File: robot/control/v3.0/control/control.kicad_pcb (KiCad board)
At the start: 2 copper layers, 0 parts

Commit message: footprint selection done, placement work
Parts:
- added BZ1: MLT-5020, AT-Buzzer:MLT-5020, F.Cu at (157.6, 175.0)
- added C1: 100n 50V, Capacitor_SMD:C_0402_1005Metric, F.Cu at (-61.0, 71.5)
- added C10: 100n 50V, Capacitor_SMD:C_0402_1005Metric, F.Cu at (-58.1, 75.5)
- added C11: 11pF, Capacitor_SMD:C_0402_1005Metric, B.Cu at (174.6, 108.3)
- added C12: 11pF, Capacitor_SMD:C_0402_1005Metric, B.Cu at (172.6, 108.3)
- added C13: 100n 50V, Capacitor_SMD:C_0402_1005Metric, F.Cu at (-58.1, 81.4)
- added C14: 2.2uF 10V, Capacitor_SMD:C_0603_1608Metric, F.Cu at (-30.6, 56.7)
- added C15: 2.2uF 10V, Capacitor_SMD:C_0603_1608Metric, F.Cu at (-30.6, 59.2)
- added C16: 100n 50V, Capacitor_SMD:C_0402_1005Metric, F.Cu at (-58.1, 83.3)
- added C17: 100n 50V, Capacitor_SMD:C_0402_1005Metric, F.Cu at (-55.2, 71.5)
- added C18: 100n 50V, Capacitor_SMD:C_0402_1005Metric, F.Cu at (-55.2, 73.5)
- added C19: 100n 50V, Capacitor_SMD:C_0402_1005Metric, F.Cu at (-55.2, 75.5)
- added C2: 1u 50V, Capacitor_SMD:C_0402_1005Metric, F.Cu at (-61.0, 73.5)
- added C20: 100n 50V, Capacitor_SMD:C_0402_1005Metric, F.Cu at (-55.2, 77.4)
- added C21: 100n 50V, Capacitor_SMD:C_0402_1005Metric, F.Cu at (-55.2, 79.4)
- added C22: 100n 50V, Capacitor_SMD:C_0402_1005Metric, F.Cu at (-55.2, 81.4)
- added C23: 100n 50V, Capacitor_SMD:C_0402_1005Metric, F.Cu at (-55.2, 83.3)
- added C24: 100n 50V, Capacitor_SMD:C_0402_1005Metric, F.Cu at (-52.3, 71.5)
- added C25: 100n 50V, Capacitor_SMD:C_0402_1005Metric, F.Cu at (-52.3, 73.5)
- added C26: 100n 50V, Capacitor_SMD:C_0402_1005Metric, F.Cu at (-52.3, 75.5)
- added C27: 100n 50V, Capacitor_SMD:C_0402_1005Metric, F.Cu at (-52.3, 77.4)
- added C28: 0.1uF 63V, Capacitor_SMD:C_0402_1005Metric, F.Cu at (154.0, 119.0)
- added C29: 0.1uF 63V, Capacitor_SMD:C_0402_1005Metric, F.Cu at (154.0, 117.0)
- added C3: 15pF, Capacitor_SMD:C_0402_1005Metric, B.Cu at (174.4, 102.6)
- added C30: 0.1u, Capacitor_SMD:C_0402_1005Metric, F.Cu at (-146.9, 131.1)
- added C31: 1u, Capacitor_SMD:C_1206_3216Metric, F.Cu at (-151.2, 127.9)
- added C32: 0.1uF 63V, Capacitor_SMD:C_0402_1005Metric, F.Cu at (-98.8, 77.4)
- added C33: 0.1uF 63V, Capacitor_SMD:C_0402_1005Metric, F.Cu at (-98.8, 79.3)
- added C34: 0.1uF 63V, Capacitor_SMD:C_0402_1005Metric, F.Cu at (-98.8, 81.3)
- added C35: 0.1uF 63V, Capacitor_SMD:C_0402_1005Metric, F.Cu at (-98.8, 83.3)
- added C36: 0.1uF 63V, Capacitor_SMD:C_0402_1005Metric, F.Cu at (-98.8, 85.2)
- added C37: 0.1uF 63V, Capacitor_SMD:C_0402_1005Metric, F.Cu at (-98.8, 87.2)
- added C38: 4.7uF 25V, Capacitor_SMD:C_0805_2012Metric, F.Cu at (163.3, 173.0)
- added C4: 15pF, Capacitor_SMD:C_0402_1005Metric, B.Cu at (172.1, 102.0)
- added C5: 100n 50V, Capacitor_SMD:C_0402_1005Metric, F.Cu at (-61.0, 79.4)
- added C6: 1u 50V, Capacitor_SMD:C_0402_1005Metric, F.Cu at (-61.0, 81.4)
- added C7: 100n 50V, Capacitor_SMD:C_0402_1005Metric, F.Cu at (-61.0, 83.3)
- added C8: 1u 50V, Capacitor_SMD:C_0402_1005Metric, F.Cu at (-58.1, 71.5)
- added C9: 1u 50V, Capacitor_SMD:C_0402_1005Metric, F.Cu at (-58.1, 73.5)
- added D1: SMBJ26CA, AT-Discrete:D_SMB_Non-Polar, F.Cu at (-152.8, 123.5)
- added D10: XL-1608UGC-04, AT-LED:LED0603, F.Cu at (-95.3, 77.7)
- added D11: XL-1608UGC-04, AT-LED:LED0603, F.Cu at (-95.3, 80.2)
- added D12: XL-1608UGC-04, AT-LED:LED0603, F.Cu at (-95.3, 82.8)
- added D13: XL-1608UGC-04, AT-LED:LED0603, F.Cu at (-95.3, 85.3)
- added D2: XL-1608UWC-04, AT-LED:LED0603, F.Cu at (-152.0, 130.8)
- added D3: LTST-C195KGJRKT, AT-LED:LED0606_S_1324, F.Cu at (95.2, 178.5)
- added D4: LTST-C195KGJRKT, AT-LED:LED0606_S_1324, F.Cu at (98.1, 178.5)
- added D5: MHT194YBCT, AT-LED:LED0606_Z_1324, F.Cu at (96.5, 182.9)
- added D6: LTST-C195KGJRKT, AT-LED:LED0606_S_1324, F.Cu at (95.2, 187.0)
- added D7: LTST-C195KGJRKT, AT-LED:LED0606_S_1324, F.Cu at (98.0, 187.0)
- added D8: XL-1608UOC-06, AT-LED:LED0603, F.Cu at (105.0, 134.4)
- added D9: RBR5LAM60ATR, Diode_SMD:D_SOD-128, F.Cu at (157.8, 169.4)
- added F1: 4A, Fuse:Fuse_1206_3216Metric_Pad1.42x1.75mm_HandSolder, F.Cu at (74.1, 128.6)
- added F2: 4A, Fuse:Fuse_1206_3216Metric_Pad1.42x1.75mm_HandSolder, F.Cu at (100.6, 64.9)
- added F3: 4A, Fuse:Fuse_1206_3216Metric_Pad1.42x1.75mm_HandSolder, F.Cu at (209.1, 74.6)
- added F4: 4A, Fuse:Fuse_1206_3216Metric_Pad1.42x1.75mm_HandSolder, F.Cu at (226.2, 142.4)
- added F5: 15A, AT-Fuses:3557-2, F.Cu at (198.5, 131.5)
- added F6: ~, Fuse:Fuse_0603_1608Metric_Pad1.05x0.95mm_HandSolder, F.Cu at (-146.8, 105.4)
- added F7: ~, Fuse:Fuse_0603_1608Metric_Pad1.05x0.95mm_HandSolder, F.Cu at (-146.8, 107.9)
- added F8: 06F-0200L1, Fuse:Fuse_0603_1608Metric_Pad1.05x0.95mm_HandSolder, F.Cu at (-146.8, 110.5)
- added H1: M3, MountingHole:MountingHole_3.2mm_M3, F.Cu at (81.0, 105.0)
- added H2: M3, MountingHole:MountingHole_3.2mm_M3, F.Cu at (219.0, 105.0)
- added H3: M3, MountingHole:MountingHole_3.2mm_M3, F.Cu at (123.0, 88.5)
- added H4: M3, MountingHole:MountingHole_3.2mm_M3, F.Cu at (176.5, 89.0)
- added J1: SD_Card_Device, AT-Connectors:MEM2067-02-180-00-A, F.Cu at (-41.2, 54.5)
- added J10: Conn_01x10_MountingPin, Connector_JST:JST_GH_SM10B-GHS-TB_1x10-1MP_P1.25mm_Horizontal, F.Cu at (126.0, 128.6)
- added J11: EC3-M, Connector_AMASS:AMASS_XT30PW-M_1x02_P2.50mm_Horizontal, F.Cu at (180.6, 118.1)
- added J12: JST-GH-SM05B, Connector_JST:JST_GH_SM05B-GHS-TB_1x05-1MP_P1.25mm_Horizontal, F.Cu at (157.1, 128.7)
- added J13: Conn_01x04, AT-Connectors:JST_PA_S04B-PASS_1x04_P2.00mm_Horizontal, F.Cu at (169.1, 126.8)
- added J14: Conn_01x06, Connector_JST:JST_GH_BM06B-GHS-TBT_1x06-1MP_P1.25mm_Vertical, F.Cu at (103.5, 141.8)
- added J15: Conn_02x05_Odd_Even, Connector_PinHeader_2.54mm:PinHeader_2x05_P2.54mm_Vertical, F.Cu at (97.6, 126.3)
- added J2: Conn_ARM_JTAG_SWD_10, AT-Connectors:Samtec-2x5pin-1.27mm, F.Cu at (-32.6, 68.2)
- added J3: SM12B-ZESS, Connector_JST:JST_ZE_SM12B-ZESS-TB_1x12-1MP_P1.50mm_Horizontal, F.Cu at (82.2, 135.5)
- added J4: BM11B-SRSS-TB, Connector_JST:JST_SH_BM11B-SRSS-TB_1x11-1MP_P1.00mm_Vertical, F.Cu at (150.5, 113.8)
- added J5: BM10B-SRSS-TB, Connector_JST:JST_SH_BM10B-SRSS-TB_1x10-1MP_P1.00mm_Vertical, F.Cu at (129.0, 116.0)
- added J6: SM12B-ZESS, Connector_JST:JST_ZE_SM12B-ZESS-TB_1x12-1MP_P1.50mm_Horizontal, F.Cu at (101.5, 75.5)
- added J7: SM12B-ZESS, Connector_JST:JST_ZE_SM12B-ZESS-TB_1x12-1MP_P1.50mm_Horizontal, F.Cu at (198.5, 75.5)
- added J8: SM12B-ZESS, Connector_JST:JST_ZE_SM12B-ZESS-TB_1x12-1MP_P1.50mm_Horizontal, F.Cu at (218.0, 135.5)
- added J9: Conn_01x10_MountingPin, Connector_JST:JST_GH_SM10B-GHS-TB_1x10-1MP_P1.25mm_Horizontal, F.Cu at (143.1, 128.6)
- added JP1: 3v0 Local Enable, AT-BoardFeatures:SolderJumper-2_2.0x1.2mm_Closed, F.Cu at (-147.0, 124.4)
- added L1: 650 @100MHz, Resistor_SMD:R_0603_1608Metric, F.Cu at (-146.6, 121.9)
- added P1: USB_C_Plug_USB2.0, Connector_USB:USB_C_Receptacle_Molex_105450-0101, F.Cu at (173.0, 66.5)
- added Q1: BSS84, Package_TO_SOT_SMD:SOT-23, F.Cu at (-30.2, 48.6)
- added Q2: BSS138K, Package_TO_SOT_SMD:SOT-23, F.Cu at (-30.2, 53.2)
- added Q3: SI2310-TP, Package_TO_SOT_SMD:SOT-23, F.Cu at (156.5, 180.9)
- added Q4: BSS138K, Package_TO_SOT_SMD:SOT-23, F.Cu at (97.7, 119.0)
- added R1: 330, Resistor_SMD:R_0402_1005Metric, F.Cu at (-36.3, 74.1)
- added R10: 1.5k, Resistor_SMD:R_0402_1005Metric, F.Cu at (-33.4, 80.0)
- added R100: 10k, Resistor_SMD:R_0402_1005Metric, F.Cu at (-107.5, 81.4)
- added R101: 10k, Resistor_SMD:R_0402_1005Metric, F.Cu at (-107.5, 83.3)
- added R102: 10k, Resistor_SMD:R_0402_1005Metric, F.Cu at (-107.5, 85.3)
- added R103: 10k, Resistor_SMD:R_0402_1005Metric, F.Cu at (-107.5, 87.3)
- added R104: 10k, Resistor_SMD:R_0402_1005Metric, F.Cu at (-107.5, 89.3)
- added R105: 10k, Resistor_SMD:R_0402_1005Metric, F.Cu at (-104.5, 77.4)
- added R106: 10k, Resistor_SMD:R_0402_1005Metric, F.Cu at (-104.5, 79.4)
- added R107: 330, Resistor_SMD:R_0402_1005Metric, F.Cu at (-104.5, 81.4)
- added R108: 10k, Resistor_SMD:R_0402_1005Metric, F.Cu at (-104.5, 83.3)
- added R109: 10k, Resistor_SMD:R_0402_1005Metric, F.Cu at (-104.5, 85.3)
- added R11: 650, Resistor_SMD:R_0402_1005Metric, F.Cu at (-33.4, 82.0)
- added R110: 10k, Resistor_SMD:R_0402_1005Metric, F.Cu at (-104.5, 87.3)
- added R111: 10k, Resistor_SMD:R_0402_1005Metric, F.Cu at (-104.5, 89.3)
- added R112: 10k, Resistor_SMD:R_0402_1005Metric, F.Cu at (-101.6, 77.4)
- added R113: 10k, Resistor_SMD:R_0402_1005Metric, F.Cu at (-101.6, 79.4)
- added R114: 330, Resistor_SMD:R_0402_1005Metric, F.Cu at (-101.6, 81.4)
- added R115: 330, Resistor_SMD:R_0402_1005Metric, F.Cu at (-101.6, 83.3)
- added R116: 10k, Resistor_SMD:R_0402_1005Metric, F.Cu at (-101.6, 85.3)
- added R117: 330, Resistor_SMD:R_0402_1005Metric, F.Cu at (-101.6, 87.3)
- added R118: 10k, Resistor_SMD:R_0402_1005Metric, F.Cu at (-101.6, 89.3)
- added R119: 100k, Resistor_SMD:R_0402_1005Metric, F.Cu at (100.9, 120.0)
- added R12: 1k, Resistor_SMD:R_0402_1005Metric, F.Cu at (-33.4, 84.0)
- added R120: 100k, Resistor_SMD:R_0402_1005Metric, F.Cu at (120.1, 113.9)
- added R121: 100k, Resistor_SMD:R_0402_1005Metric, F.Cu at (120.1, 115.9)
- added R122: 330, Resistor_SMD:R_0402_1005Metric, F.Cu at (120.1, 117.8)
- added R123: 330, Resistor_SMD:R_0402_1005Metric, F.Cu at (120.1, 119.8)
- added R124: 100k, Resistor_SMD:R_0402_1005Metric, F.Cu at (120.1, 121.8)
- added R125: 100k, Resistor_SMD:R_0402_1005Metric, F.Cu at (120.1, 123.8)
- added R13: 1k, Resistor_SMD:R_0402_1005Metric, F.Cu at (-30.5, 74.1)
- added R14: 1k, Resistor_SMD:R_0402_1005Metric, F.Cu at (-30.5, 76.1)
- added R15: 5.1k, Resistor_SMD:R_0402_1005Metric, F.Cu at (-30.5, 78.1)
- added R16: 100k, Resistor_SMD:R_0402_1005Metric, F.Cu at (74.7, 124.2)
- added R17: 100k, Resistor_SMD:R_0402_1005Metric, F.Cu at (72.7, 124.2)
- added R18: 330, Resistor_SMD:R_0402_1005Metric, F.Cu at (70.8, 124.2)
- added R19: 330, Resistor_SMD:R_0402_1005Metric, F.Cu at (68.8, 124.2)
- added R2: 10k, Resistor_SMD:R_0402_1005Metric, F.Cu at (-36.3, 76.1)
- added R20: 100k, Resistor_SMD:R_0402_1005Metric, F.Cu at (66.8, 124.2)
- added R21: 100k, Resistor_SMD:R_0402_1005Metric, F.Cu at (64.8, 124.2)
- added R22: 330, Resistor_SMD:R_0402_1005Metric, F.Cu at (146.0, 121.5)
- added R23: 330, Resistor_SMD:R_0402_1005Metric, F.Cu at (146.0, 119.5)
- added R24: 10k, Resistor_SMD:R_0402_1005Metric, F.Cu at (146.0, 117.5)
- added R25: 10k, Resistor_SMD:R_0402_1005Metric, F.Cu at (146.0, 115.5)
- added R26: 100k, Resistor_SMD:R_0402_1005Metric, F.Cu at (104.2, 62.2)
- added R27: 100k, Resistor_SMD:R_0402_1005Metric, F.Cu at (102.8, 60.8)
- added R28: 330, Resistor_SMD:R_0402_1005Metric, F.Cu at (101.4, 59.4)
- added R29: 330, Resistor_SMD:R_0402_1005Metric, F.Cu at (100.0, 58.0)
- added R3: 10k, Resistor_SMD:R_0402_1005Metric, F.Cu at (-36.3, 78.1)
- added R30: 100k, Resistor_SMD:R_0402_1005Metric, F.Cu at (98.6, 56.6)
- added R31: 100k, Resistor_SMD:R_0402_1005Metric, F.Cu at (97.2, 55.2)
- added R32: 100k, Resistor_SMD:R_0402_1005Metric, F.Cu at (211.8, 78.2)
- added R33: 100k, Resistor_SMD:R_0402_1005Metric, F.Cu at (213.2, 76.8)
- added R34: 330, Resistor_SMD:R_0402_1005Metric, F.Cu at (214.6, 75.4)
- added R35: 330, Resistor_SMD:R_0402_1005Metric, F.Cu at (216.0, 74.0)
- added R36: 100k, Resistor_SMD:R_0402_1005Metric, F.Cu at (217.4, 72.6)
- added R37: 100k, Resistor_SMD:R_0402_1005Metric, F.Cu at (220.9, 71.7)
- added R38: 100k, Resistor_SMD:R_0402_1005Metric, F.Cu at (225.5, 146.8)
- added R39: 100k, Resistor_SMD:R_0402_1005Metric, F.Cu at (227.5, 146.8)
- added R4: 100k, Resistor_SMD:R_0402_1005Metric, F.Cu at (-36.3, 80.0)
- added R40: 330, Resistor_SMD:R_0402_1005Metric, F.Cu at (229.5, 146.8)
- added R41: 330, Resistor_SMD:R_0402_1005Metric, F.Cu at (231.5, 146.8)
- added R42: 100k, Resistor_SMD:R_0402_1005Metric, F.Cu at (233.5, 146.8)
- added R43: 100k, Resistor_SMD:R_0402_1005Metric, F.Cu at (235.4, 146.8)
- added R44: 100k, Resistor_SMD:R_0402_1005Metric, F.Cu at (147.5, 135.7)
- added R45: 100k, Resistor_SMD:R_0402_1005Metric, F.Cu at (147.5, 137.7)
- added R46: 330, Resistor_SMD:R_0402_1005Metric, F.Cu at (147.5, 139.7)
- added R47: 330, Resistor_SMD:R_0402_1005Metric, F.Cu at (147.5, 141.7)
- added R48: 100k, Resistor_SMD:R_0402_1005Metric, F.Cu at (147.5, 143.7)
- added R49: 100k, Resistor_SMD:R_0402_1005Metric, F.Cu at (147.5, 145.7)
- added R5: 1k, Resistor_SMD:R_0402_1005Metric, F.Cu at (-36.3, 82.0)
- added R50: 100k, Resistor_SMD:R_0402_1005Metric, F.Cu at (126.4, 135.8)
- added R51: 100k, Resistor_SMD:R_0402_1005Metric, F.Cu at (126.4, 137.8)
- added R52: 330, Resistor_SMD:R_0402_1005Metric, F.Cu at (126.4, 139.8)
- added R53: 330, Resistor_SMD:R_0402_1005Metric, F.Cu at (126.4, 141.8)
- added R54: 100k, Resistor_SMD:R_0402_1005Metric, F.Cu at (126.4, 143.8)
- added R55: 100k, Resistor_SMD:R_0402_1005Metric, F.Cu at (126.4, 145.8)
- added R56: 100k, Resistor_SMD:R_0402_1005Metric, F.Cu at (-155.5, 127.2)
- added R57: 23.7k, Resistor_SMD:R_0402_1005Metric, F.Cu at (-155.5, 129.2)
- added R58: 330, Resistor_SMD:R_0402_1005Metric, F.Cu at (-155.5, 131.2)
- added R59: 330, Resistor_SMD:R_0402_1005Metric, F.Cu at (-111.3, 140.0)
- added R6: 1k, Resistor_SMD:R_0402_1005Metric, F.Cu at (-36.3, 84.0)
- added R60: 330, Resistor_SMD:R_0402_1005Metric, F.Cu at (-111.3, 142.0)
- added R61: 2.7k, Resistor_SMD:R_0402_1005Metric, F.Cu at (-111.3, 143.9)
- added R62: 2.7k, Resistor_SMD:R_0402_1005Metric, F.Cu at (-111.3, 145.9)
- added R63: 330, Resistor_SMD:R_0402_1005Metric, F.Cu at (-111.3, 147.9)
- added R64: 330, Resistor_SMD:R_0402_1005Metric, F.Cu at (-111.3, 149.9)
- added R65: 10k, Resistor_SMD:R_0402_1005Metric, F.Cu at (-111.3, 151.9)
- added R66: 10k, Resistor_SMD:R_0402_1005Metric, F.Cu at (-108.4, 140.0)
- added R67: 10k, Resistor_SMD:R_0402_1005Metric, F.Cu at (-108.4, 142.0)
- added R68: 10k, Resistor_SMD:R_0402_1005Metric, F.Cu at (-108.4, 143.9)
- added R69: 10k, Resistor_SMD:R_0402_1005Metric, F.Cu at (-108.4, 145.9)
- added R7: 100k, Resistor_SMD:R_0402_1005Metric, F.Cu at (-33.4, 74.1)
- added R70: 10k, Resistor_SMD:R_0402_1005Metric, F.Cu at (-108.4, 147.9)
- added R71: 10k, Resistor_SMD:R_0402_1005Metric, F.Cu at (-108.4, 149.9)
- added R72: 10k, Resistor_SMD:R_0402_1005Metric, F.Cu at (-108.4, 151.9)
- added R73: 10k, Resistor_SMD:R_0402_1005Metric, F.Cu at (-105.5, 140.0)
- added R74: 330, Resistor_SMD:R_0402_1005Metric, F.Cu at (-105.5, 142.0)
- added R75: 330, Resistor_SMD:R_0402_1005Metric, F.Cu at (-105.5, 143.9)
- added R76: 10k, Resistor_SMD:R_0402_1005Metric, F.Cu at (-105.5, 145.9)
- added R77: 10k, Resistor_SMD:R_0402_1005Metric, F.Cu at (-105.5, 147.9)
- added R78: 10k, Resistor_SMD:R_0402_1005Metric, F.Cu at (-105.5, 149.9)
- added R79: 10k, Resistor_SMD:R_0402_1005Metric, F.Cu at (-105.5, 151.9)
- added R8: 100k, Resistor_SMD:R_0402_1005Metric, F.Cu at (-33.4, 76.1)
- added R80: 10k, Resistor_SMD:R_0402_1005Metric, F.Cu at (-102.5, 140.0)
- added R81: 10k, Resistor_SMD:R_0402_1005Metric, F.Cu at (-102.5, 142.0)
- added R82: 10k, Resistor_SMD:R_0402_1005Metric, F.Cu at (-102.5, 143.9)
- added R83: 10k, Resistor_SMD:R_0402_1005Metric, F.Cu at (-102.5, 145.9)
- added R84: 330, Resistor_SMD:R_0402_1005Metric, F.Cu at (-113.3, 77.4)
- added R85: 330, Resistor_SMD:R_0402_1005Metric, F.Cu at (-113.3, 79.4)
- added R86: 330, Resistor_SMD:R_0402_1005Metric, F.Cu at (-113.3, 81.4)
- added R87: 10k, Resistor_SMD:R_0402_1005Metric, F.Cu at (-113.3, 83.3)
- added R88: 10k, Resistor_SMD:R_0402_1005Metric, F.Cu at (-113.3, 85.3)
- added R89: 330, Resistor_SMD:R_0402_1005Metric, F.Cu at (-113.3, 87.3)
- added R9: 11.5k, Resistor_SMD:R_0402_1005Metric, F.Cu at (-33.4, 78.1)
- added R90: 330, Resistor_SMD:R_0402_1005Metric, F.Cu at (-113.3, 89.3)
- added R91: 10, Resistor_SMD:R_0402_1005Metric, F.Cu at (-110.4, 77.4)
- added R92: 330, Resistor_SMD:R_0402_1005Metric, F.Cu at (-110.4, 79.4)
- added R93: 330, Resistor_SMD:R_0402_1005Metric, F.Cu at (-110.4, 81.4)
- added R94: 330, Resistor_SMD:R_0402_1005Metric, F.Cu at (-110.4, 83.3)
- added R95: 330, Resistor_SMD:R_0402_1005Metric, F.Cu at (-110.4, 85.3)
- added R96: 10k, Resistor_SMD:R_0402_1005Metric, F.Cu at (-110.4, 87.3)
- added R97: 330, Resistor_SMD:R_0402_1005Metric, F.Cu at (-110.4, 89.3)
- added R98: 10k, Resistor_SMD:R_0402_1005Metric, F.Cu at (-107.5, 77.4)
- added R99: 10k, Resistor_SMD:R_0402_1005Metric, F.Cu at (-107.5, 79.4)
- added SW1: A6SN-1104, Button_Switch_SMD:SW_DIP_SPSTx01_Slide_Omron_A6S-110x_W8.9mm_P2.54mm, F.Cu at (142.0, 68.0)
- added SW10: B3F-1000, at-switches:B3F-1000, F.Cu at (188.0, 103.5)
- added SW11: B3F-1000, at-switches:B3F-1000, F.Cu at (208.0, 103.5)
- added SW12: B3F-1000, at-switches:B3F-1000, F.Cu at (198.0, 111.5)
- added SW2: RST, Button_Switch_SMD:SW_SPST_TL3305A, F.Cu at (-44.5, 81.3)
- added SW3: SW_DIP_x02, at-switches:219-2MST, F.Cu at (182.5, 68.0)
- added SW4: 221ADC16, at-switches:221ADC16, F.Cu at (132.0, 68.0)
- added SW5: SW_DIP_x02, at-switches:219-2MST, F.Cu at (122.5, 68.0)
- added SW6: 219-8MST, at-switches:219-8MST, F.Cu at (156.0, 68.0)
- added SW7: B3F-1000, at-switches:B3F-1000, F.Cu at (188.0, 111.5)
- added SW8: B3F-1000, at-switches:B3F-1000, F.Cu at (198.1, 103.5)
- added SW9: B3F-1000, at-switches:B3F-1000, F.Cu at (198.1, 95.4)
- added U1: STM32H723ZGTx, Package_QFP:LQFP-144_20x20mm_P0.5mm, B.Cu at (150.0, 105.0)
- added U10: SK9822, AT-LED:SK9822, F.Cu at (-101.9, 65.1)
- added U11: SK9822, AT-LED:SK9822, F.Cu at (-101.9, 72.6)
- added U12: SK9822, AT-LED:SK9822, F.Cu at (-93.4, 50.0)
- added U13: SK9822, AT-LED:SK9822, F.Cu at (-93.4, 57.5)
- added U14: SK9822, AT-LED:SK9822, F.Cu at (-93.4, 65.1)
- added U2: BMI323, AT-IMU:BMI323, F.Cu at (150.0, 118.8)
- added U3: TLV70030_SOT353, Package_TO_SOT_SMD:SOT-353_SC-70-5, F.Cu at (-146.3, 128.2)
- added U4: SK9822, AT-LED:SK9822, F.Cu at (-110.5, 50.0)
- added U5: SK9822, AT-LED:SK9822, F.Cu at (-110.5, 57.5)
- added U6: SK9822, AT-LED:SK9822, F.Cu at (-110.5, 65.1)
- added U7: SK9822, AT-LED:SK9822, F.Cu at (-110.5, 72.6)
- added U8: SK9822, AT-LED:SK9822, F.Cu at (-101.9, 50.0)
- added U9: SK9822, AT-LED:SK9822, F.Cu at (-101.9, 57.5)
- added Y1: Q13FC13500005, Crystal:Crystal_SMD_3215-2Pin_3.2x1.5mm, B.Cu at (168.7, 102.1)
- added Y2: TAXM8M4RDBCCT2T, Crystal:Crystal_SMD_3225-4Pin_3.2x2.5mm, B.Cu at (168.2, 107.2)

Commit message: very coarse control placement
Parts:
- removed F5: 15A, AT-Fuses:3557-2
- C28, C29, C30, C31, C38, D1, D9, F8, J1, JP1, L1, Q3, R120, R121, R122, R123, R124, R125, R16, R17, R18, R19, R20, R21, R22, R23, R24, R25, R26, R27, R28, R29, R30, R31, R32, R33, R34, R35, R36, R37, R38, R39, R40, R41, R42, R43, R44, R45, R46, R47, R48, R49, R50, R51, R52, R53, R54, R55, R56, R58, U3: moved to B.Cu
- J11: footprint Connector_AMASS:AMASS_XT30PW-M_1x02_P2.50mm_Horizontal -> Connector_AMASS:AMASS_XT30U-M_1x02_P5.0mm_Vertical
- moved R57 350.2 mm to (194.7, 133.7)
- moved D2 349.5 mm to (197.5, 133.7)
- moved F8 338.9 mm to (191.7, 127.9)
- moved U7 336.6 mm to (220.6, 133.4), turned to 90 degrees
- moved L1 335.4 mm to (188.8, 130.3)
- moved R58 335.4 mm to (179.9, 123.7)
- moved D1 335.4 mm to (182.6, 128.8)
- moved U3 335.4 mm to (189.1, 124.0)
- moved C31 335.4 mm to (184.1, 124.3)
- moved JP1 335.4 mm to (188.3, 127.9)
- moved R56 335.4 mm to (179.9, 125.0)
- moved F7 329.5 mm to (182.6, 118.0), turned to 90 degrees
- moved F6 327.6 mm to (180.6, 118.0), turned to 90 degrees
- moved C30 327.0 mm to (180.0, 122.4)
- moved U6 322.6 mm to (211.5, 85.0), turned to 45 degrees
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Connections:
- J11 pad 2: +V_{BATT(RAW)} -> +BATT
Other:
- copper layers 2 -> 6

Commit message: initial coase placement done
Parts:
- added H5: M2, MountingHole:MountingHole_2.2mm_M2_DIN965_Pad, F.Cu at (115.5, 89.5)
- added H6: M2, MountingHole:MountingHole_2.2mm_M2_DIN965_Pad, F.Cu at (87.5, 89.5)
- added H7: M2, MountingHole:MountingHole_2.2mm_M2_DIN965_Pad, F.Cu at (115.5, 129.5)
- added H8: M2, MountingHole:MountingHole_2.2mm_M2_DIN965_Pad, F.Cu at (87.5, 129.5)
- F6, F7, J11, Q4, R119: moved to B.Cu
- moved J2 88.9 mm to (197.0, 52.0)
- moved SW2 88.7 mm to (188.0, 52.0)
- moved U5 18.6 mm to (106.5, 83.0)
- moved R21 14.8 mm to (80.6, 144.5), turned to 90 degrees
- moved R119 13.8 mm to (96.3, 133.0)
- moved Q4 13.1 mm to (99.5, 132.0)
- moved R20 12.9 mm to (82.5, 144.5), turned to 90 degrees
- moved R19 11.4 mm to (84.5, 144.5), turned to 90 degrees
- moved R16 10.7 mm to (90.5, 144.5), turned to 90 degrees
- moved R18 10.4 mm to (86.5, 144.5), turned to 90 degrees
- moved R17 10.2 mm to (88.5, 144.5), turned to 90 degrees
- moved F1 5.80 mm to (84.0, 134.5)
- moved U4 3.70 mm to (79.5, 133.5)
- moved D6 3.24 mm to (98.2, 107.0)
- moved F7 2.79 mm to (180.0, 119.0)
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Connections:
- J15 pad 1: +5V -> Net-(J15-Pin_1)
- J15 pad 3: /display/LCD.RX -> GND
- J15 pad 4: unconnected-(J15-Pin_4-Pad4) -> GND
- J15 pad 7: GND -> /display/LCD.RX
- J15 pad 8: GND -> unconnected-(J15-Pin_8-Pad8)
- J15 pad 9: Net-(J15-Pin_9) -> +5V
- Q4 pad 3: Net-(J15-Pin_9) -> Net-(J15-Pin_1)
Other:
- board outline added: 148 x 86 mm

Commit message: load board config and profiles
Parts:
- moved SW4 2.00 mm to (130.5, 71.0)
- moved SW5 2.00 mm to (121.0, 71.0)
- moved SW6 2.00 mm to (148.5, 71.0)
- moved SW1 1.80 mm to (164.9, 71.0)
- moved SW3 1.80 mm to (182.4, 71.0)
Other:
- board text added: "A"
- board text added: "B"
- board text added: "BOOT"
- board text added: "BOT NUM"
- board text added: "CONFIG"
- board text added: "DBG"
- board text added: "KICKER"
- board text added: "LV PWR"
- board text added: "ON"
- board text added: "OPTICAL"
- board text added: "PWR TELEM"
- board text added: "RADIO"
- board text added: "U"
- board text added: "WiFi"
- board text added: "Y"
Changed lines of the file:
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@@
 	(generator_version "8.0")
 	(general
-		(thickness 1.6)
+		(thickness 1.5284)
 		(legacy_teardrops no)
 	)
 	(paper "A4")
+	(title_block
+		(date "2025-01-25")
+	)
 	(layers
 		(0 "F.Cu" signal)
@@
 			(layer "dielectric 1"
 				(type "prepreg")
-				(thickness 0.1)
-				(material "FR4")
-				(epsilon_r 4.5)
-				(loss_tangent 0.02)
+				(color "FR4 natural")
+				(thickness 0.0994)
+				(material "3313")
+				(epsilon_r 4.05)
+				(loss_tangent 0)
 			)
 			(layer "In1.Cu"
 				(type "copper")
-				(thickness 0.035)
+				(thickness 0.0152)
 			)
 			(layer "dielectric 2"
 				(type "core")
+				(color "FR4 natural")
 				(thickness 0.535)
-				(material "FR4")
-				(epsilon_r 4.5)
-				(loss_tangent 0.02)
+				(material "Core")
+				(epsilon_r 4.6)
+				(loss_tangent 0)
 			)
 			(layer "In2.Cu"
 				(type "copper")
-				(thickness 0.035)
+				(thickness 0.0152)
 			)
 			(layer "dielectric 3"
 				(type "prepreg")
-				(thickness 0.1)
-				(material "FR4")
-				(epsilon_r 4.5)
-				(loss_tangent 0.02)
+				(color "FR4 natural")
+				(thickness 0.1088)
+				(material "2116")
+				(epsilon_r 4.25)
+				(loss_tangent 0)
 			)
 			(layer "In3.Cu"
 				(type "copper")
-				(thickness 0.035)
+				(thickness 0.0152)
 			)
 			(layer "dielectric 4"
 				(type "core")
+				(color "FR4 natural")
 				(thickness 0.535)
-				(material "FR4")
-				(epsilon_r 4.5)
-				(loss_tangent 0.02)
+				(material "Core")
+				(epsilon_r 4.6)
+				(loss_tangent 0)
 			)
 			(layer "In4.Cu"
 				(type "copper")
-				(thickness 0.035)
+				(thickness 0.0152)
 			)
 			(layer "dielectric 5"
 				(type "prepreg")
-				(thickness 0.1)
-				(material "FR4")
-				(epsilon_r 4.5)
-				(loss_tangent 0.02)
+				(color "FR4 natural")
+				(thickness 0.0994)
+				(material "3313")
+				(epsilon_r 4.05)
+				(loss_tangent 0)
 			)
 			(layer "B.Cu"
@@
 	(footprint "at-switches:219-2MST"
 		(layer "F.Cu")
-		(at 182.4 72.8 -90)
+		(at 182.4 71 -90)
 		(descr "SMD 2x-dip-switch SPST , Slide, row spacing 8.61 mm (338 mils), body size 6.7x6.55mm (see e.g. https://www.ctscorp.com/wp-content/uploads/219.pdf), SMD, LowProfile")
 		(property "Reference" "SW3"
@@
 	(footprint "at-switches:219-8MST"
 		(layer "F.Cu")
-		(at 148.5 73 -90)
+		(at 148.5 71 -90)
 		(descr "SMD 8x-dip-switch SPST , Slide, row spacing 8.61 mm (338 mils), body size 6.7x21.88mm (see e.g. https://www.ctscorp.com/wp-content/uploads/219.pdf), SMD, LowProfile")
 		(property "Reference" "SW6"
@@
 	(footprint "at-switches:221ADC16"
 		(layer "F.Cu")
-		(at 130.5 73 180)
+		(at 130.5 71 180)
 		(property "Reference" "SW4"
-			(at 0 -6 360)
+			(at 0 -6 0)
 			(layer "F.SilkS")
 			(effects
@@
 		)
 		(property "Value" "221ADC16"
-			(at 0 6 360)
+			(at 0 6 0)
 			(layer "F.Fab")
 			(effects
@@
 		)
 		(property "Footprint" "at-switches:221ADC16"
-			(at 0 0 360)
+			(at 0 0 0)
 			(layer "F.Fab")
 			(hide yes)
@@
 		)
 		(property "Datasheet" "https://www.ctscorp.com/wp-content/uploads/221.pdf"
-			(at 0 0 360)
+			(at 0 0 0)
 			(layer "F.Fab")
 			(hide yes)
@@
 		)
 		(property "Description" ""
-			(at 0 0 360)
+			(at 0 0 0)
 			(layer "F.Fab")
 			(hide yes)
@@
 		)
 		(fp_text user "${REFERENCE}"
-			(at 0 0 360)
+			(at 0 0 0)
 			(layer "F.Fab")
 			(effects
@@
 	(footprint "at-switches:219-2MST"
 		(layer "F.Cu")
-		(at 121 73 -90)
+		(at 121 71 -90)
 		(descr "SMD 2x-dip-switch SPST , Slide, row spacing 8.61 mm (338 mils), body size 6.7x6.55mm (see e.g. https://www.ctscorp.com/wp-content/uploads/219.pdf), SMD, LowProfile")
 		(property "Reference" "SW5"
@@
 	(footprint "Button_Switch_SMD:SW_DIP_SPSTx01_Slide_Omron_A6S-110x_W8.9mm_P2.54mm"
 		(layer "F.Cu")
-		(at 164.9 72.8 90)
+		(at 164.9 71 90)
 		(descr "SMD 1x-dip-switch SPST Omron_A6S-110x, Slide, row spacing 8.9 mm (350 mils), body size  (see http://omronfs.omron.com/en_US/ecb/products/pdf/en-a6s.pdf)")
 		(tags "SMD DIP Switch SPST Slide 8.9mm 350mil")
@@
 		(layer "Edge.Cuts")
 	)
+	(gr_text "OPTICAL"
+		(at 140.5 131 0)
+		(layer "F.SilkS" knockout)
+		(effects
+			(font
+				(size 1 1)
+				(thickness 0.2)
+			)
+		)
+	)
+	(gr_text "BOT NUM"
+		(at 130.5 63 180)
+		(layer "F.SilkS" knockout)
+		(effects
+			(font
+				(size 1 1)
+				(thickness 0.2)
+			)
+		)
+	)
+	(gr_text "RADIO"
+		(at 125 131 0)
+		(layer "F.SilkS" knockout)
+		(effects
+			(font
+				(size 1 1)
+				(thickness 0.2)
+			)
+		)
+	)
+	(gr_text "B"
+		(at 122.5 63.5 180)
+		(layer "F.SilkS")
+		(effects
+			(font
+				(size 2 2)
+				(thickness 0.3)
+			)
+		)
+	)
+	(gr_text "DBG"
+		(at 165 63 180)
+		(layer "F.SilkS" knockout)
+		(effects
+			(font
+				(size 1 1)
+				(thickness 0.2)
+			)
+		)
+	)
+	(gr_text "LV PWR"
+		(at 183.5 131 0)
+		(layer "F.SilkS" knockout)
+		(effects
+			(font
+				(size 1 1)
+				(thickness 0.2)
+			)
+		)
+	)
+	(gr_text "BOOT"
+		(at 182.5 63 180)
+		(layer "F.SilkS" knockout)
+		(effects
+			(font
+				(size 1 1)
+				(thickness 0.2)
+			)
+		)
+	)
+	(gr_text "A"
+		(at 119.5 78.5 180)
+		(layer "F.SilkS")
+		(effects
+			(font
+				(size 2 2)
+				(thickness 0.3)
+			)
+		)
+	)
+	(gr_text "Y"
+		(at 122.5 78.5 180)
+		(layer "F.SilkS")
+		(effects
+			(font
+				(size 2 2)
+				(thickness 0.3)
+			)
+		)
+	)
+	(gr_text "KICKER"
+		(at 157.5 131 0)
+		(layer "F.SilkS" knockout)
+		(effects
+			(font
+				(size 1 1)
+				(thickness 0.2)
+			)
+		)
+	)
+	(gr_text "WiFi\n"
+		(at 153.5 78.5 180)
+		(layer "F.SilkS")
+		(effects
+			(font
+				(size 2 2)
+				(thickness 0.3)
+			)
+		)
+	)
+	(gr_text "U"
+		(at 119.5 63.5 180)
+		(layer "F.SilkS")
+		(effects
+			(font
+				(size 2 2)
+				(thickness 0.3)
+			)
+		)
+	)
+	(gr_text "ON"
+		(at 165 78 180)
+		(layer "F.SilkS")
+		(effects
+			(font
+				(size 2 2)
+				(thickness 0.3)
+			)
+		)
+	)
+	(gr_text "CONFIG"
+		(at 148.5 63 180)
+		(layer "F.SilkS" knockout)
+		(effects
+			(font
+				(size 1 1)
+				(thickness 0.2)
+			)
+		)
+	)
+	(gr_text "PWR TELEM"
+		(at 171.5 131 0)
+		(layer "F.SilkS" knockout)
+		(effects
+			(font
+				(size 1 1)
+				(thickness 0.2)
+			)
+		)
+	)
 	(zone

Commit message: Initial decoupling caps and some resistor placement
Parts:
- C1, C10, C14, C15, C16, C17, C18, C19, C2, C20, C21, C22, C23, C24, C25, C26, C27, C32, C33, C34, C35, C36, C37, C5, C6, C7, C8, C9, Q1, Q2, R1, R10, R11, R12, R13, R14, R2, R3, R4, R5, R6, R7, R8, R9: moved to B.Cu
- moved C13 115.8 mm to (222.0, 94.5)
- moved C8 87.0 mm to (164.0, 113.0)
- moved C18 85.3 mm to (158.0, 118.5), turned to -90 degrees
- moved C32 83.8 mm to (188.0, 111.0), turned to 180 degrees
- moved C9 83.3 mm to (164.0, 110.5)
- moved C10 82.5 mm to (164.0, 111.5)
- moved C17 82.5 mm to (164.0, 109.5)
- moved C19 80.6 mm to (151.5, 118.5), turned to -90 degrees
- moved C7 80.2 mm to (164.0, 114.0)
- moved C14 80.1 mm to (143.2, 118.8), turned to -90 degrees
- moved C20 76.8 mm to (146.5, 118.5), turned to -90 degrees
- moved C37 76.2 mm to (196.5, 110.5), turned to 180 degrees
- moved C33 76.1 mm to (196.5, 102.5), turned to 180 degrees
- moved C36 74.7 mm to (206.0, 102.5), turned to 180 degrees
- moved C21 73.2 mm to (141.5, 118.5), turned to -90 degrees
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
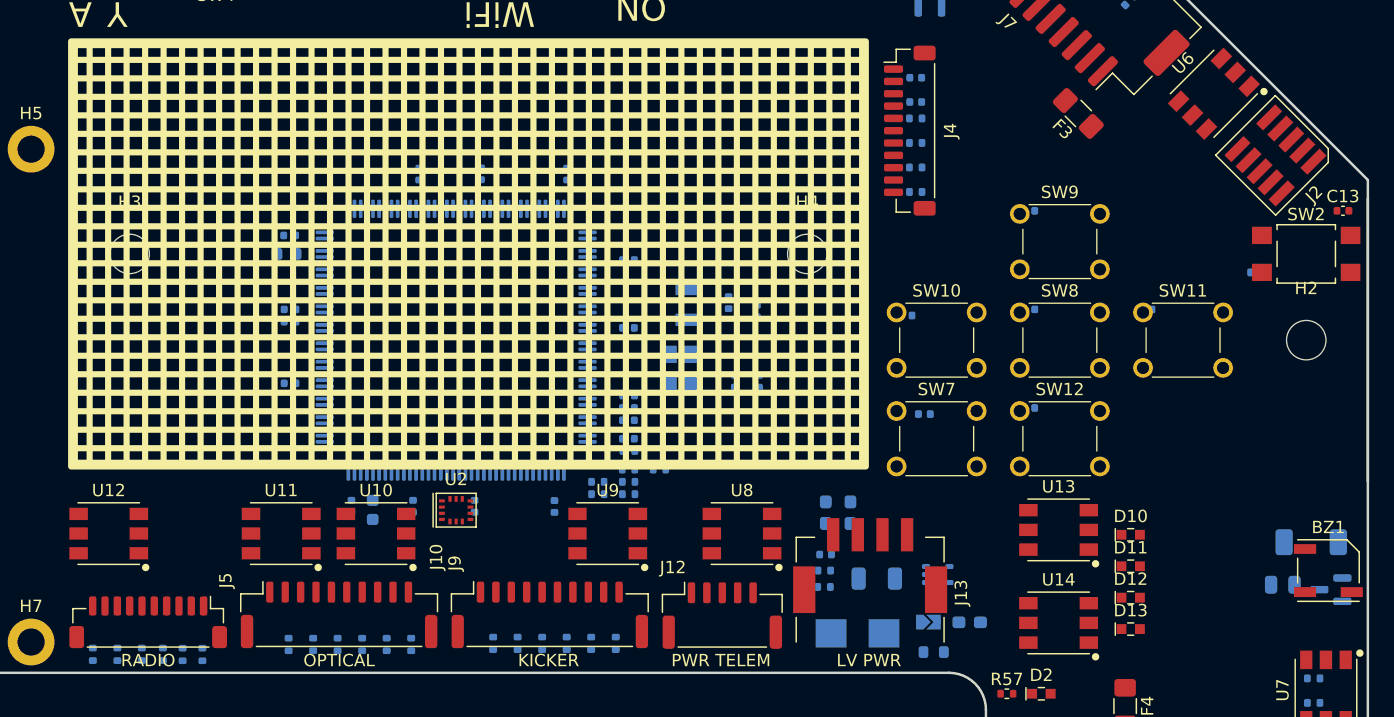
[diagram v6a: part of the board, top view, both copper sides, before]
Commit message: Placing and routing capacitors near control MCU
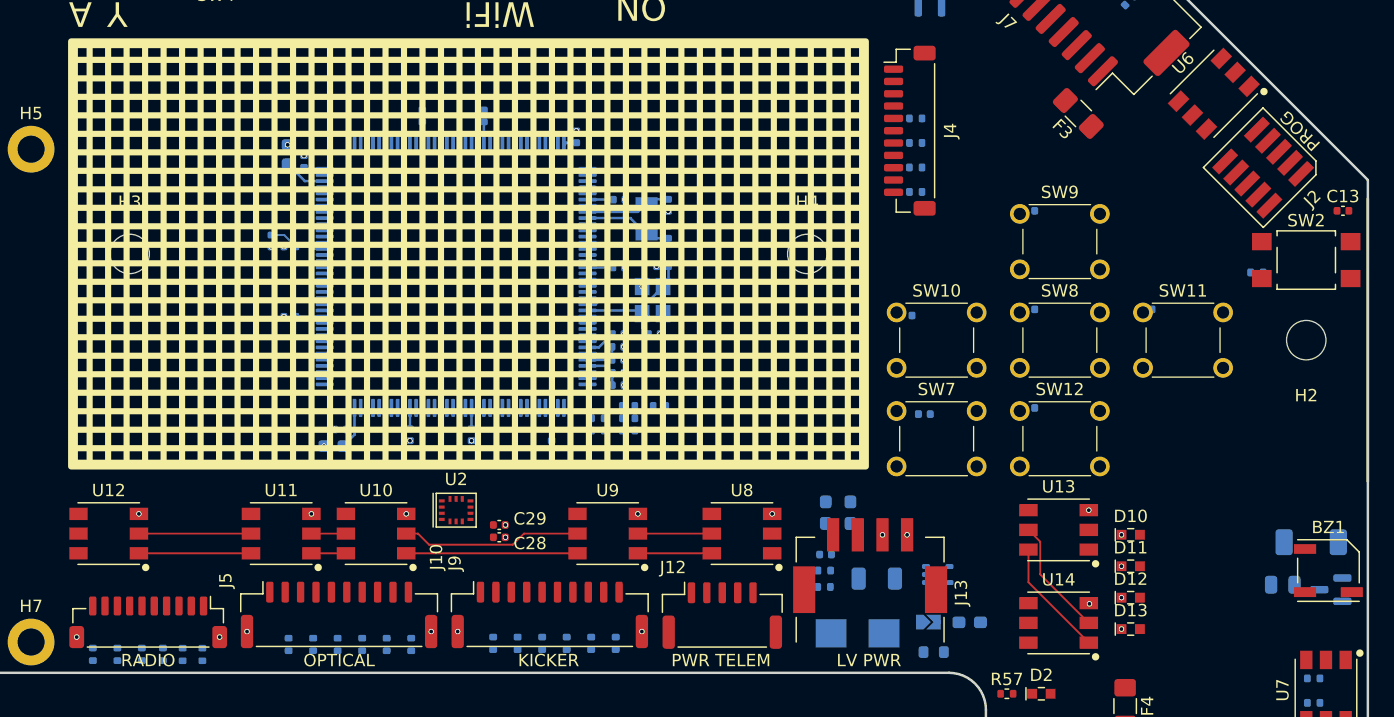
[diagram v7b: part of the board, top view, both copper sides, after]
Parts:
- C28, C29: moved to F.Cu
- moved C29 49.6 mm to (153.5, 120.0)
- moved C28 48.9 mm to (153.5, 121.0)
- moved C12 11.0 mm to (166.8, 99.0), turned to 180 degrees
- moved C3 9.64 mm to (167.2, 96.2)
- moved C11 9.33 mm to (166.1, 104.5), turned to 0 degrees
- moved C4 9.31 mm to (167.2, 94.0), turned to -90 degrees
- moved C15 8.08 mm to (136.3, 89.9), turned to 90 degrees
- moved Y1 7.67 mm to (165.4, 95.2), turned to -90 degrees
- moved C6 6.72 mm to (135.0, 97.0), turned to -90 degrees
- moved C7 6.41 mm to (163.2, 107.7)
- moved C21 6.29 mm to (140.6, 112.2), turned to 180 degrees
- moved C23 6.11 mm to (137.7, 90.5), turned to 90 degrees
- moved C14 6.07 mm to (140.1, 113.6), turned to 180 degrees
- moved Y2 5.92 mm to (165.9, 101.8)
- moved C18 5.82 mm to (157.8, 112.7)
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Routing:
- net +3V3: track 0.00 -> 27.6 mm
- net Net-(U10-CKI): track 0.00 -> 14.6 mm
- net Net-(U10-SDI): track 0.00 -> 13.9 mm
- net Net-(U13-SDO): track 0.00 -> 9.58 mm
- net Net-(U13-CKO): track 0.00 -> 9.58 mm
- net Net-(U11-SDO): track 0.00 -> 9.10 mm
- net Net-(U11-CKO): track 0.00 -> 9.10 mm
- net /mcu/RCC_OSC_P: track 0.00 -> 8.56 mm
- net /mcu/RCC_OSC32_N: track 0.00 -> 7.68 mm
- net /mcu/RCC_OSC32_P: track 0.00 -> 7.43 mm
- net /mcu/RCC_OSC_N: track 0.00 -> 6.40 mm
- net +3V0: track 0.00 -> 6.28 mm
- net Net-(U8-SDO): track 0.00 -> 6.00 mm
- net Net-(U8-CKO): track 0.00 -> 6.00 mm
- net Net-(C15-Pad1): track 0.00 -> 3.59 mm
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- added copper zone on In3.Cu, net GND
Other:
- board text added: "PROG"
